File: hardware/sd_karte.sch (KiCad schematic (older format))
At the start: 11 parts, among them CON1 SD_Card

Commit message: Allen Bauteilen Footprints zugeordnet.
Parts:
- D1, D2: footprint Diodes_ThroughHole:Diode_DO-35_SOD27_Horizontal_RM10 -> Diodes_THT:D_DO-35_SOD27_P7.62mm_Horizontal
- R2, R3, R4, R7, R8, R9: footprint Resistors_ThroughHole:Resistor_Horizontal_RM10mm -> Discret:R4-5
- R5, R6: footprint (none) -> Discret:R4-5
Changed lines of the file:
@@
 F 0 "D1" H 4450 4150 50  0000 C CNN
 F 1 "1N4148" H 4450 3950 50  0000 C CNN
-F 2 "Diodes_ThroughHole:Diode_DO-35_SOD27_Horizontal_RM10" H 4450 4050 60  0001 C CNN
+F 2 "Diodes_THT:D_DO-35_SOD27_P7.62mm_Horizontal" H 4450 4050 60  0001 C CNN
 F 3 "" H 4450 4050 60  0000 C CNN
 	1    4450 4050
@@
 F 0 "D2" H 4450 4550 50  0000 C CNN
 F 1 "1N4148" H 4450 4350 50  0000 C CNN
-F 2 "Diodes_ThroughHole:Diode_DO-35_SOD27_Horizontal_RM10" H 4450 4450 60  0001 C CNN
+F 2 "Diodes_THT:D_DO-35_SOD27_P7.62mm_Horizontal" H 4450 4450 60  0001 C CNN
 F 3 "" H 4450 4450 60  0000 C CNN
 	1    4450 4450
@@
 F 0 "R7" V 3780 3150 50  0000 C CNN
 F 1 "1,8k" V 3700 3150 50  0000 C CNN
-F 2 "Resistors_ThroughHole:Resistor_Horizontal_RM10mm" V 3630 3150 30  0001 C CNN
+F 2 "Discret:R4-5" V 3630 3150 30  0001 C CNN
 F 3 "" H 3700 3150 30  0000 C CNN
 	1    3700 3150
@@
 F 0 "R8" V 3980 3250 50  0000 C CNN
 F 1 "1,8k" V 3900 3250 50  0000 C CNN
-F 2 "Resistors_ThroughHole:Resistor_Horizontal_RM10mm" V 3830 3250 30  0001 C CNN
+F 2 "Discret:R4-5" V 3830 3250 30  0001 C CNN
 F 3 "" H 3900 3250 30  0000 C CNN
 	1    3900 3250
@@
 F 0 "R9" V 3780 3550 50  0000 C CNN
 F 1 "1,8k" V 3700 3550 50  0000 C CNN
-F 2 "Resistors_ThroughHole:Resistor_Horizontal_RM10mm" V 3630 3550 30  0001 C CNN
+F 2 "Discret:R4-5" V 3630 3550 30  0001 C CNN
 F 3 "" H 3700 3550 30  0000 C CNN
 	1    3700 3550
@@
 F 0 "R2" V 3980 2900 50  0000 C CNN
 F 1 "3,3k" V 3900 2900 50  0000 C CNN
-F 2 "Resistors_ThroughHole:Resistor_Horizontal_RM10mm" V 3830 2900 30  0001 C CNN
+F 2 "Discret:R4-5" V 3830 2900 30  0001 C CNN
 F 3 "" H 3900 2900 30  0000 C CNN
 	1    3900 2900
@@
 F 0 "R3" V 4180 2900 50  0000 C CNN
 F 1 "3,3k" V 4100 2900 50  0000 C CNN
-F 2 "Resistors_ThroughHole:Resistor_Horizontal_RM10mm" V 4030 2900 30  0001 C CNN
+F 2 "Discret:R4-5" V 4030 2900 30  0001 C CNN
 F 3 "" H 4100 2900 30  0000 C CNN
 	1    4100 2900
@@
 F 0 "R4" V 4380 2900 50  0000 C CNN
 F 1 "3,3k" V 4300 2900 50  0000 C CNN
-F 2 "Resistors_ThroughHole:Resistor_Horizontal_RM10mm" V 4230 2900 30  0001 C CNN
+F 2 "Discret:R4-5" V 4230 2900 30  0001 C CNN
 F 3 "" H 4300 2900 30  0000 C CNN
 	1    4300 2900
@@
 F 0 "R5" V 6830 2950 50  0000 C CNN
 F 1 "47k" V 6750 2950 50  0000 C CNN
-F 2 "" V 6680 2950 50  0001 C CNN
+F 2 "Discret:R4-5" V 6680 2950 50  0001 C CNN
 F 3 "" H 6750 2950 50  0001 C CNN
 	1    6750 2950
@@
 F 0 "R6" V 7080 2950 50  0000 C CNN
 F 1 "47kR" V 7000 2950 50  0000 C CNN
-F 2 "" V 6930 2950 50  0001 C CNN
+F 2 "Discret:R4-5" V 6930 2950 50  0001 C CNN
 F 3 "" H 7000 2950 50  0001 C CNN
 	1    7000 2950

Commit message: - Hardware nochmal angepasst - erstes Layout erstellt - Schaltplan auf Rev.1.3.4 gesetzt
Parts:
- removed CON1: SD_Card, w_conn_misc:sd_socket, symbol SD_Card
- added SD1: SD_Socket, ka_sd_sockets:SD_Socket_104D-TCA0-R06, symbol SD_Socket
- renumbered R5 to R2, R6 to R3, R2 to R4, R3 to R5, R4 to R6
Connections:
- wire segments 28 -> 31
- no-connect marks 4 -> 2
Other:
- moved on the sheet: R2, R3
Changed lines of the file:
@@
 EESchema Schematic File Version 2
+LIBS:power
+LIBS:ka_library
 LIBS:1541-rebuild-rescue
-LIBS:power
 LIBS:device
 LIBS:transistors
@@
 LIBS:w_transistor
 LIBS:w_vacuum
-LIBS:kattanek
 LIBS:1541-rebuild-cache
 EELAYER 25 0
@@
 Sheet 2 4
 Title "1541-rebuid"
-Date "2018-05-06"
-Rev "1.3.3"
+Date "2018-05-08"
+Rev "1.3.4"
 Comp ""
 Comment1 "Erstellt von: Thorsten Kattanek"
@@
 Comment4 ""
 $EndDescr
-$Comp
-L SD_Card CON1
-U 1 1 55F7A1C8
-P 5700 3450
-F 0 "CON1" H 5050 4000 50  0000 C CNN
-F 1 "SD_Card" H 6300 2900 50  0000 C CNN
-F 2 "w_conn_misc:sd_socket" H 5900 3800 50  0001 C CNN
-F 3 "" H 5700 3450 60  0000 C CNN
-	1    5700 3450
-	1    0    0    -1
-$EndComp
-$Comp
-L GND #PWR014
-U 1 1 55F7A326
-P 4700 3900
-F 0 "#PWR014" H 4700 3650 50  0001 C CNN
-F 1 "GND" H 4700 3750 50  0000 C CNN
-F 2 "" H 4700 3900 60  0000 C CNN
-F 3 "" H 4700 3900 60  0000 C CNN
-	1    4700 3900
-	1    0    0    -1
-$EndComp
 $Comp
 L D D1
@@
 $EndComp
 NoConn ~ 4800 3850
-NoConn ~ 6600 3550
-NoConn ~ 6600 3650
 Text HLabel 3250 3750 0    60   Input ~ 0
 MISO
@@
 U 1 1 55F7B36C
 P 3700 3150
-F 0 "R7" V 3780 3150 50  0000 C CNN
+F 0 "R7" V 3600 3150 50  0000 C CNN
 F 1 "1,8k" V 3700 3150 50  0000 C CNN
 F 2 "Discret:R4-5" V 3630 3150 30  0001 C CNN
@@
 $EndComp
 $Comp
-L R R2
+L R R4
 U 1 1 55F7BA6C
 P 3900 2900
-F 0 "R2" V 3980 2900 50  0000 C CNN
+F 0 "R4" V 3980 2900 50  0000 C CNN
 F 1 "3,3k" V 3900 2900 50  0000 C CNN
 F 2 "Discret:R4-5" V 3830 2900 30  0001 C CNN
@@
 $EndComp
 $Comp
-L R R3
+L R R5
 U 1 1 55F7BC20
 P 4100 2900
-F 0 "R3" V 4180 2900 50  0000 C CNN
+F 0 "R5" V 4180 2900 50  0000 C CNN
 F 1 "3,3k" V 4100 2900 50  0000 C CNN
 F 2 "Discret:R4-5" V 4030 2900 30  0001 C CNN
@@
 $EndComp
 $Comp
-L R R4
+L R R6
 U 1 1 55F7BCCD
 P 4300 2900
-F 0 "R4" V 4380 2900 50  0000 C CNN
+F 0 "R6" V 4380 2900 50  0000 C CNN
 F 1 "3,3k" V 4300 2900 50  0000 C CNN
 F 2 "Discret:R4-5" V 4230 2900 30  0001 C CNN
@@
 	1    0    0    -1
 $EndComp
-$Comp
-L GND #PWR016
-U 1 1 55F7BE30
+Wire Wire Line
+	4450 4300 4450 4200
+Wire Wire Line
+	4800 3450 4450 3450
+Wire Wire Line
+	4450 3450 4450 3900
+Wire Wire Line
+	4450 4600 4450 4700
+Wire Wire Line
+	4800 3750 3250 3750
+Wire Wire Line
+	3250 3150 3550 3150
+Wire Wire Line
+	3850 3150 4800 3150
+Wire Wire Line
+	4050 3250 4800 3250
+Wire Wire Line
+	3750 3250 3250 3250
+Wire Wire Line
+	3250 3550 3550 3550
+Wire Wire Line
+	3850 3550 4800 3550
+Wire Wire Line
+	3900 3050 3900 3150
+Connection ~ 3900 3150
+Wire Wire Line
+	4100 3050 4100 3250
+Connection ~ 4100 3250
+Wire Wire Line
+	4300 3050 4300 3550
+Connection ~ 4300 3550
+Wire Wire Line
+	4100 2500 4100 2750
+Wire Wire Line
+	4300 2600 4300 2750
+Wire Wire Line
+	3900 2600 4300 2600
+Connection ~ 4100 2600
+Wire Wire Line
+	3900 2750 3900 2600
+Wire Wire Line
+	4800 3350 4700 3350
+Wire Wire Line
+	4700 3350 4700 3900
+Wire Wire Line
+	4800 3650 4700 3650
+Connection ~ 4700 3650
+$Comp
+L R R2
+U 1 1 5ADB73A5
+P 6650 2750
+F 0 "R2" V 6730 2750 50  0000 C CNN
+F 1 "47k" V 6650 2750 50  0000 C CNN
+F 2 "Discret:R4-5" V 6580 2750 50  0001 C CNN
+F 3 "" H 6650 2750 50  0001 C CNN
+	1    6650 2750
+	1    0    0    -1
+$EndComp
+$Comp
+L R R3
+U 1 1 5ADB753C
+P 6900 2750
+F 0 "R3" V 6980 2750 50  0000 C CNN
+F 1 "47kR" V 6900 2750 50  0000 C CNN
+F 2 "Discret:R4-5" V 6830 2750 50  0001 C CNN
+F 3 "" H 6900 2750 50  0001 C CNN
+	1    6900 2750
+	1    0    0    -1
+$EndComp
+$Comp
+L +5V #PWR016
+U 1 1 5ADB75CA
+P 6650 2400
+F 0 "#PWR016" H 6650 2250 50  0001 C CNN
+F 1 "+5V" H 6650 2540 50  0000 C CNN
+F 2 "" H 6650 2400 60  0000 C CNN
+F 3 "" H 6650 2400 60  0000 C CNN
+	1    6650 2400
+	1    0    0    -1
+$EndComp
+Wire Wire Line
+	6650 2400 6650 2600
+Wire Wire Line
+	6650 2500 6900 2500
+Wire Wire Line
+	6900 2500 6900 2600
+Connection ~ 6650 2500
+Text HLabel 7150 3150 2    60   Input ~ 0
+SD_DETECT
+Text HLabel 7150 3050 2    60   Input ~ 0
+SD_WP
+Wire Wire Line
+	6500 3050 7150 3050
+Wire Wire Line
+	7150 3150 6500 3150
+Wire Wire Line
+	6650 2900 6650 3050
+Connection ~ 6650 3050
+Wire Wire Line
+	6900 2900 6900 3150
+Connection ~ 6900 3150
+Text Notes 650  7650 0    60   ~ 0
+SD_DETECT ist LO wenn eine Karte eingestekt ist\nSD_WP ist LO wenn Schreibschutz aktiv\n(SD_WP muss HI sein damit man schreiben kann)
+$Comp
+L GND #PWR017
+U 1 1 5AF0D189
 P 4100 2500
-F 0 "#PWR016" H 4100 2250 50  0001 C CNN
+F 0 "#PWR017" H 4100 2250 50  0001 C CNN
 F 1 "GND" H 4100 2350 50  0000 C CNN
-F 2 "" H 4100 2500 60  0000 C CNN
-F 3 "" H 4100 2500 60  0000 C CNN
+F 2 "" H 4100 2500 50  0001 C CNN
+F 3 "" H 4100 2500 50  0001 C CNN
 	1    4100 2500
 	-1   0    0    1
 $EndComp
-Wire Wire Line
-	4450 4300 4450 4200
-Wire Wire Line
-	4800 3450 4450 3450
-Wire Wire Line
-	4450 3450 4450 3900
-Wire Wire Line
-	4450 4600 4450 4700
-Wire Wire Line
-	4800 3750 3250 3750
-Wire Wire Line
-	3250 3150 3550 3150
-Wire Wire Line
-	3850 3150 4800 3150
-Wire Wire Line
-	4050 3250 4800 3250
-Wire Wire Line
-	3750 3250 3250 3250
-Wire Wire Line
-	3250 3550 3550 3550
-Wire Wire Line
-	3850 3550 4800 3550
-Wire Wire Line
-	3900 3050 3900 3150
-Connection ~ 3900 3150
-Wire Wire Line
-	4100 3050 4100 3250
-Connection ~ 4100 3250
-Wire Wire Line
-	4300 3050 4300 3550
-Connection ~ 4300 3550
-Wire Wire Line
-	4100 2500 4100 2750
-Wire Wire Line
-	4300 2600 4300 2750
-Wire Wire Line
-	3900 2600 4300 2600
-Connection ~ 4100 2600
-Wire Wire Line
-	3900 2750 3900 2600
-Wire Wire Line
-	4800 3350 4700 3350
-Wire Wire Line
-	4700 3350 4700 3900
-Wire Wire Line
-	4800 3650 4700 3650
-Connection ~ 4700 3650
-$Comp
-L R R5
-U 1 1 5ADB73A5
-P 6750 2950
-F 0 "R5" V 6830 2950 50  0000 C CNN
-F 1 "47k" V 6750 2950 50  0000 C CNN
-F 2 "Discret:R4-5" V 6680 2950 50  0001 C CNN
-F 3 "" H 6750 2950 50  0001 C CNN
-	1    6750 2950
-	1    0    0    -1
-$EndComp
-$Comp
-L R R6
-U 1 1 5ADB753C
-P 7000 2950
-F 0 "R6" V 7080 2950 50  0000 C CNN
-F 1 "47kR" V 7000 2950 50  0000 C CNN
-F 2 "Discret:R4-5" V 6930 2950 50  0001 C CNN
-F 3 "" H 7000 2950 50  0001 C CNN
-	1    7000 2950
-	1    0    0    -1
-$EndComp
-$Comp
-L +5V #PWR017
-U 1 1 5ADB75CA
-P 6750 2600
-F 0 "#PWR017" H 6750 2450 50  0001 C CNN
-F 1 "+5V" H 6750 2740 50  0000 C CNN
-F 2 "" H 6750 2600 60  0000 C CNN
-F 3 "" H 6750 2600 60  0000 C CNN
-	1    6750 2600
-	1    0    0    -1
-$EndComp
-Wire Wire Line
-	6750 2600 6750 2800
-Wire Wire Line
-	6750 2700 7000 2700
-Wire Wire Line
-	7000 2700 7000 2800
-Connection ~ 6750 2700
-Text HLabel 7250 3250 2    60   Input ~ 0
-SD_DETECT
-Text HLabel 7250 3350 2    60   Input ~ 0
-SD_WP
-Wire Wire Line
-	6600 3250 7250 3250
-Wire Wire Line
-	7250 3350 6600 3350
-Wire Wire Line
-	6750 3100 6750 3250
-Connection ~ 6750 3250
-Wire Wire Line
-	7000 3100 7000 3350
-Connection ~ 7000 3350
-Text Notes 650  7650 0    60   ~ 0
-SD_DETECT ist LO wenn eine Karte eingestekt ist\nSD_WP ist LO wenn Schreibschutz aktiv\n(SD_WP muss HI sein damit man schreiben kann)
+$Comp
+L GND #PWR018
+U 1 1 5AF0D222
+P 4700 3900
+F 0 "#PWR018" H 4700 3650 50  0001 C CNN
+F 1 "GND" H 4700 3750 50  0000 C CNN
+F 2 "" H 4700 3900 50  0001 C CNN
+F 3 "" H 4700 3900 50  0001 C CNN
+	1    4700 3900
+	1    0    0    -1
+$EndComp
+$Comp
+L SD_Socket SD1
+U 1 1 5AF0A85D
+P 5650 3450
+F 0 "SD1" H 5650 3950 60  0000 C CNN
+F 1 "SD_Socket" H 5700 3250 60  0000 C CNN
+F 2 "ka_sd_sockets:SD_Socket_104D-TCA0-R06" H 3800 2100 60  0001 C CNN
+F 3 "" H 3800 2100 60  0001 C CNN
+	1    5650 3450
+	1    0    0    -1
+$EndComp
+Wire Wire Line
+	6500 3250 6550 3250
+Wire Wire Line
+	6550 3250 6550 3900
+Wire Wire Line
+	6550 3850 6500 3850
+$Comp
+L GND #PWR019
+U 1 1 5AF0AE1C
+P 6550 3900
+F 0 "#PWR019" H 6550 3650 50  0001 C CNN
+F 1 "GND" H 6550 3750 50  0000 C CNN
+F 2 "" H 6550 3900 50  0001 C CNN
+F 3 "" H 6550 3900 50  0001 C CNN
+	1    6550 3900
+	1    0    0    -1
+$EndComp
+Connection ~ 6550 3850
 $EndSCHEMATC

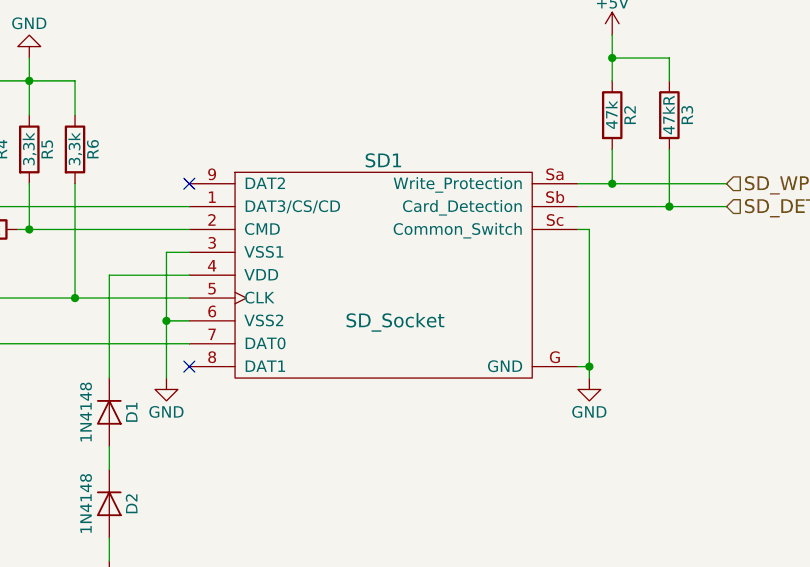
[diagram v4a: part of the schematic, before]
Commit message: Borad fertig gestellt und auf rev 1.3.5 gesetzt Gerberfiles erzeugt und als rar gepackt. Mit PCB Hersteller -Seedstudio- getestet.
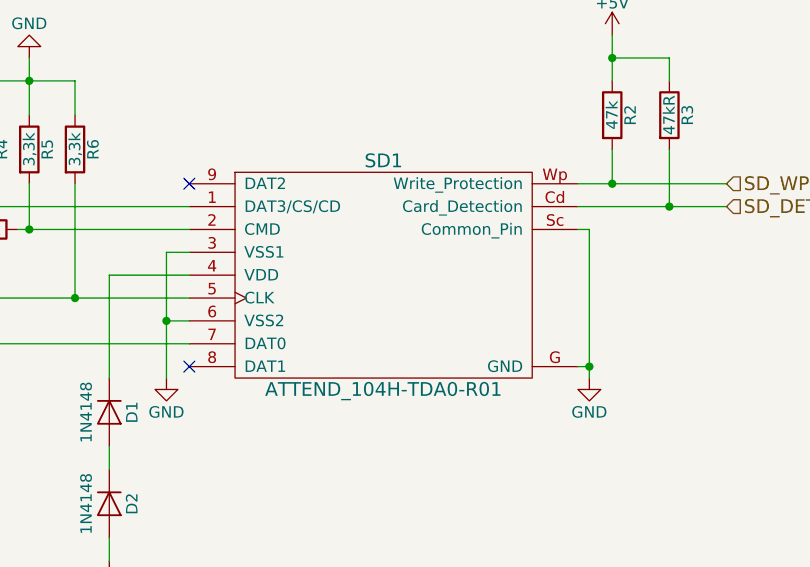
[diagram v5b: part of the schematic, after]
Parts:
- removed SD1: SD_Socket, ka_sd_sockets:SD_Socket_104D-TCA0-R06, symbol SD_Socket
- added SD1: ATTEND_104H-TDA0-R01, ka_sd_sockets:ATTEND_104H-TDA0-R01, symbol ATTEND_104H-TDA0-R01
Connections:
- net GND: now also SD1.3 (VSS1), SD1.6 (VSS2), SD1.G (GND), SD1.Sc (Common_Pin)
- net MISO: now also SD1.7 (DAT0)
- net SD_DETECT: now also SD1.Cd (Card_Detection)
- net SD_WP: now also SD1.Wp (Write_Protection)
- net at D1.1 (K): now also SD1.4 (VDD)
- net at R4.2, R7.1: now also SD1.1 (DAT3/CS/CD)
- net at R5.2, R8.1: now also SD1.2 (CMD)
- net at R6.2, R9.1: now also SD1.5 (CLK)
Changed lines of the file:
@@
 EESchema Schematic File Version 2
 LIBS:power
-LIBS:ka_library
 LIBS:1541-rebuild-rescue
 LIBS:device
@@
 LIBS:w_transistor
 LIBS:w_vacuum
+LIBS:ka_sd_sockets
 LIBS:1541-rebuild-cache
 EELAYER 25 0
@@
 Sheet 2 4
 Title "1541-rebuid"
-Date "2018-05-08"
-Rev "1.3.4"
+Date "2018-05-11"
+Rev "1.3.5"
 Comp ""
 Comment1 "Erstellt von: Thorsten Kattanek"
@@
 	1    0    0    -1
 $EndComp
-$Comp
-L SD_Socket SD1
-U 1 1 5AF0A85D
-P 5650 3450
-F 0 "SD1" H 5650 3950 60  0000 C CNN
-F 1 "SD_Socket" H 5700 3250 60  0000 C CNN
-F 2 "ka_sd_sockets:SD_Socket_104D-TCA0-R06" H 3800 2100 60  0001 C CNN
-F 3 "" H 3800 2100 60  0001 C CNN
-	1    5650 3450
-	1    0    0    -1
-$EndComp
 Wire Wire Line
 	6500 3250 6550 3250
@@
 $EndComp
 Connection ~ 6550 3850
+$Comp
+L ATTEND_104H-TDA0-R01 SD1
+U 1 1 5AF5BDB3
+P 5650 3450
+F 0 "SD1" H 5650 3950 60  0000 C CNN
+F 1 "ATTEND_104H-TDA0-R01" H 5650 2950 60  0000 C CNN
+F 2 "ka_sd_sockets:ATTEND_104H-TDA0-R01" H 3800 2100 60  0001 C CNN
+F 3 "" H 3800 2100 60  0001 C CNN
+	1    5650 3450
+	1    0    0    -1
+$EndComp
 $EndSCHEMATC
